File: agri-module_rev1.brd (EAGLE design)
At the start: 160 x 100 mm, 38 parts, among them M1 DMG1023, U2 PCA9570, U3 APDS-9960

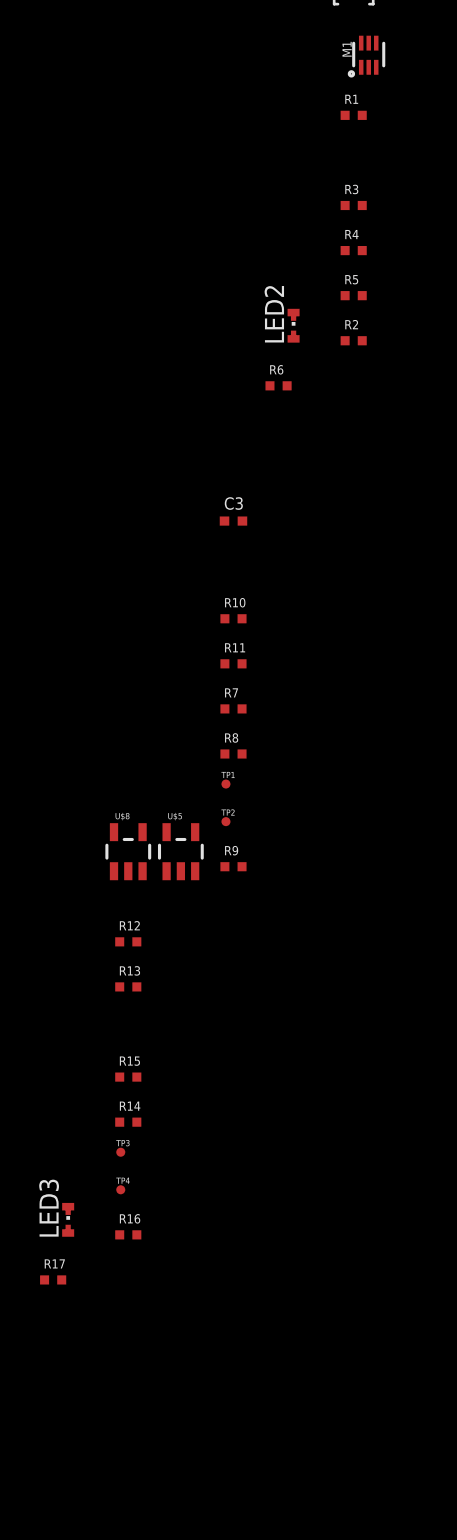
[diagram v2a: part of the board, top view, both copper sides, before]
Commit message: Added indication use for one of LEDs
-also connected EC_pow correctly
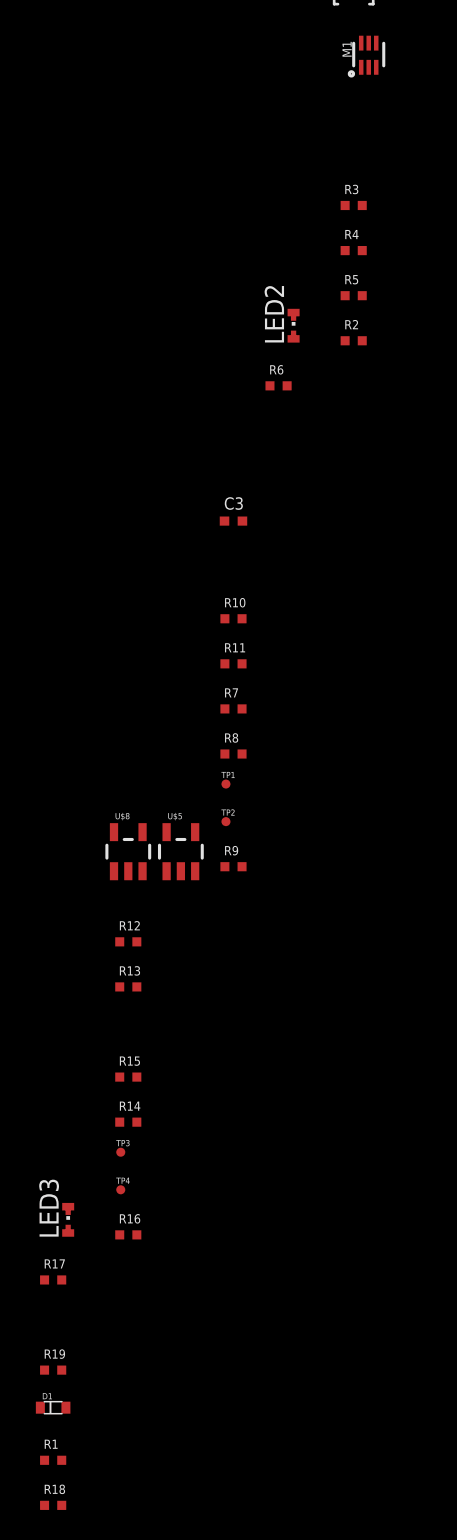
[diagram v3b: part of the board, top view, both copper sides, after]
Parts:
- added D1: DB2S205, EAP - Library:SSMINI2-F5-B
- added R18: 10k, BrainGrid - Resistors:R0402-BG
- added R19: 100R, BrainGrid - Resistors:R0402-BG
- R1: value 100R -> 10k
- moved R1 91.7 mm to (-126.0, -139.0)
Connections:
- removed net N$6: LED2.A@1, U$4.6
- new net LED_INDICATE: D1.C, LED2.A@1, U$4.6
- net 3.6V_HP: now also R1.1, R18.1
- net GEST_LED: now also R19.2, U3.5; no longer R1.2
- net N$4: now also D1.A, R19.1; no longer R1.1, U3.5
- net N$7: now also R18.2
- net N$8: now also R1.2
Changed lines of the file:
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@@
 <attribute name="VMAX" value="-20V" x="-105" y="-45.5" size="1.778" layer="27" display="off"/>
-</element>
-<element name="R1" library="BrainGrid - Resistors" package="R0402-BG" value="100R" x="-106" y="-49.5">
-<attribute name="MPN" value="RC0402JR-07100RL" x="-106" y="-49.5" size="1.778" layer="27" display="off"/>
-<attribute name="ALTMPN" value="RC1005J101CS" x="-106" y="-49.5" size="1.778" layer="27" display="off"/>
-<attribute name="MANF" value="Yageo" x="-106" y="-49.5" size="1.778" layer="27" display="off"/>
-<attribute name="TEMPCO" value="±100ppm/°C" x="-106" y="-49.5" size="1.778" layer="27" display="off"/>
-<attribute name="VPN" value="311-100JRCT-ND" x="-106" y="-49.5" size="1.778" layer="27" display="off"/>
-<attribute name="VENDOR" value="Digikey" x="-106" y="-49.5" size="1.778" layer="27" display="off"/>
-<attribute name="ALTMANF" value="Samsung" x="-106" y="-49.5" size="1.778" layer="27" display="off"/>
-<attribute name="PACKAGE" value="0402" x="-106" y="-49.5" size="1.778" layer="27" display="off"/>
-<attribute name="POPULATE" value="" x="-106" y="-49.5" size="1.778" layer="27" display="off"/>
-<attribute name="TOLERANCE" value="±5%" x="-106" y="-49.5" size="1.778" layer="27" display="off"/>
 </element>
 <element name="R3" library="BrainGrid - Resistors" package="R0402-BG" value="10k" x="-106" y="-55.5">
@@
 <attribute name="POPULATE" value="DNP" x="-126" y="-127" size="1.778" layer="27" display="off"/>
 <attribute name="TOLERANCE" value="" x="-126" y="-127" size="1.778" layer="27" display="off"/>
+</element>
+<element name="R19" library="BrainGrid - Resistors" package="R0402-BG" value="100R" x="-126" y="-133">
+<attribute name="MPN" value="RC0402JR-07100RL" x="-126" y="-133" size="1.778" layer="27" display="off"/>
+<attribute name="ALTMPN" value="RC1005J101CS" x="-126" y="-133" size="1.778" layer="27" display="off"/>
+<attribute name="MANF" value="Yageo" x="-126" y="-133" size="1.778" layer="27" display="off"/>
+<attribute name="TEMPCO" value="±100ppm/°C" x="-126" y="-133" size="1.778" layer="27" display="off"/>
+<attribute name="VPN" value="311-100JRCT-ND" x="-126" y="-133" size="1.778" layer="27" display="off"/>
+<attribute name="VENDOR" value="Digikey" x="-126" y="-133" size="1.778" layer="27" display="off"/>
+<attribute name="ALTMANF" value="Samsung" x="-126" y="-133" size="1.778" layer="27" display="off"/>
+<attribute name="PACKAGE" value="0402" x="-126" y="-133" size="1.778" layer="27" display="off"/>
+<attribute name="POPULATE" value="DNP" x="-126" y="-133" size="1.778" layer="27" display="off"/>
+<attribute name="TOLERANCE" value="±5%" x="-126" y="-133" size="1.778" layer="27" display="off"/>
+</element>
+<element name="D1" library="EAP - Library" package="SSMINI2-F5-B" value="DB2S205" x="-126" y="-135.5">
+<attribute name="MPN" value="" x="-126" y="-135.5" size="1.778" layer="27" display="off"/>
+<attribute name="HEIGHT" value="" x="-126" y="-135.5" size="1.778" layer="27" display="off"/>
+<attribute name="ALTMPN" value="" x="-126" y="-135.5" size="1.778" layer="27" display="off"/>
+<attribute name="MANF" value="" x="-126" y="-135.5" size="1.778" layer="27" display="off"/>
+<attribute name="VPN" value="" x="-126" y="-135.5" size="1.778" layer="27" display="off"/>
+<attribute name="VENDOR" value="" x="-126" y="-135.5" size="1.778" layer="27" display="off"/>
+<attribute name="ALTMANF" value="" x="-126" y="-135.5" size="1.778" layer="27" display="off"/>
+<attribute name="PACKAGE" value="" x="-126" y="-135.5" size="1.778" layer="27" display="off"/>
+<attribute name="POPULATE" value="DNP" x="-126" y="-135.5" size="1.778" layer="27" display="off"/>
+<attribute name="DNP" value="" x="-126" y="-135.5" size="1.778" layer="27" display="off"/>
+<attribute name="TOLERANCE" value="" x="-126" y="-135.5" size="1.778" layer="27" display="off"/>
+</element>
+<element name="R1" library="BrainGrid - Resistors" package="R0402-BG" value="10k" x="-126" y="-139">
+<attribute name="MPN" value="RC0402JR-0710KL" x="-126" y="-139" size="1.778" layer="27" display="off"/>
+<attribute name="ALTMPN" value="1622826-4" x="-126" y="-139" size="1.778" layer="27" display="off"/>
+<attribute name="MANF" value="Yageo" x="-126" y="-139" size="1.778" layer="27" display="off"/>
+<attribute name="TEMPCO" value="±100ppm/°C" x="-126" y="-139" size="1.778" layer="27" display="off"/>
+<attribute name="VPN" value="311-10KJRCT-ND" x="-126" y="-139" size="1.778" layer="27" display="off"/>
+<attribute name="VENDOR" value="Digikey" x="-126" y="-139" size="1.778" layer="27" display="off"/>
+<attribute name="ALTMANF" value="TE" x="-126" y="-139" size="1.778" layer="27" display="off"/>
+<attribute name="PACKAGE" value="0402" x="-126" y="-139" size="1.778" layer="27" display="off"/>
+<attribute name="POPULATE" value="" x="-126" y="-139" size="1.778" layer="27" display="off"/>
+<attribute name="TOLERANCE" value="±5%" x="-126" y="-139" size="1.778" layer="27" display="off"/>
+</element>
+<element name="R18" library="BrainGrid - Resistors" package="R0402-BG" value="10k" x="-126" y="-142">
+<attribute name="MPN" value="RC0402JR-0710KL" x="-126" y="-142" size="1.778" layer="27" display="off"/>
+<attribute name="ALTMPN" value="1622826-4" x="-126" y="-142" size="1.778" layer="27" display="off"/>
+<attribute name="MANF" value="Yageo" x="-126" y="-142" size="1.778" layer="27" display="off"/>
+<attribute name="TEMPCO" value="±100ppm/°C" x="-126" y="-142" size="1.778" layer="27" display="off"/>
+<attribute name="VPN" value="311-10KJRCT-ND" x="-126" y="-142" size="1.778" layer="27" display="off"/>
+<attribute name="VENDOR" value="Digikey" x="-126" y="-142" size="1.778" layer="27" display="off"/>
+<attribute name="ALTMANF" value="TE" x="-126" y="-142" size="1.778" layer="27" display="off"/>
+<attribute name="PACKAGE" value="0402" x="-126" y="-142" size="1.778" layer="27" display="off"/>
+<attribute name="POPULATE" value="" x="-126" y="-142" size="1.778" layer="27" display="off"/>
+<attribute name="TOLERANCE" value="±5%" x="-126" y="-142" size="1.778" layer="27" display="off"/>
 </element>
 </elements>
@@
 <contactref element="U$2" pad="3"/>
 <contactref element="U$5" pad="5"/>
+<contactref element="R1" pad="1"/>
+<contactref element="R18" pad="1"/>
 <wire x1="-105.43" y1="-64.5" x2="-118.45" y2="-97.1999" width="0" layer="19" extent="1-1"/>
 <wire x1="-105.43" y1="-61.5" x2="-105.43" y2="-64.5" width="0" layer="19" extent="1-1"/>
@@
 <wire x1="-98.405" y1="-19.5" x2="-102.6" y2="-39.45" width="0" layer="19" extent="1-1"/>
 <wire x1="-67.405" y1="-1.5" x2="-98.405" y2="-19.5" width="0" layer="19" extent="1-1"/>
+<wire x1="-126.57" y1="-139" x2="-118.45" y2="-97.1999" width="0" layer="19" extent="1-1"/>
+<wire x1="-126.57" y1="-142" x2="-126.57" y2="-139" width="0" layer="19" extent="1-1"/>
 </signal>
 <signal name="N$18">
@@
 </signal>
 <signal name="EC_POW">
+<contactref element="TP2" pad="TP"/>
 <contactref element="U2" pad="6"/>
-<contactref element="TP2" pad="TP"/>
 <wire x1="-101.4" y1="-40" x2="-114.5" y2="-96.5" width="0" layer="19" extent="1-1"/>
 </signal>
@@
 <wire x1="-105.3" y1="-40.485" x2="-105.3" y2="-41.455" width="0" layer="19" extent="1-1"/>
 </signal>
-<signal name="N$4">
-<contactref element="U3" pad="5"/>
-<contactref element="R1" pad="1"/>
-<wire x1="-106.7" y1="-41.455" x2="-106.57" y2="-49.5" width="0" layer="19" extent="1-1"/>
-</signal>
 <signal name="N$5">
 <contactref element="U$4" pad="7"/>
@@
 <wire x1="-32.5" y1="-15.3" x2="-40.5" y2="-19.5" width="0" layer="19" extent="1-1"/>
 </signal>
-<signal name="N$6">
+<signal name="LED_INDICATE">
 <contactref element="U$4" pad="6"/>
 <contactref element="LED2" pad="A@1"/>
+<contactref element="D1" pad="C"/>
+<wire x1="-126.85" y1="-135.5" x2="-110" y2="-64" width="0" layer="19" extent="1-1"/>
 <wire x1="-32" y1="-15.3" x2="-110" y2="-64" width="0" layer="19" extent="1-1"/>
 </signal>
@@
 <contactref element="U$2" pad="6"/>
 <contactref element="U$6" pad="8"/>
+<contactref element="R1" pad="2"/>
 <wire x1="-88.05" y1="-21.825" x2="-94.595" y2="-19.5" width="0" layer="19" extent="1-1"/>
+<wire x1="-125.43" y1="-139" x2="-88.05" y2="-21.825" width="0" layer="19" extent="1-1"/>
 </signal>
 <signal name="N$7">
 <contactref element="U$6" pad="7"/>
 <contactref element="U$2" pad="4"/>
+<contactref element="R18" pad="2"/>
 <wire x1="-87.325" y1="-21.825" x2="-97.135" y2="-19.5" width="0" layer="19" extent="1-1"/>
+<wire x1="-125.43" y1="-142" x2="-97.135" y2="-19.5" width="0" layer="19" extent="1-1"/>
 </signal>
 <signal name="N$10">
@@
 <signal name="GEST_LED">
 <contactref element="U2" pad="4"/>
-<contactref element="R1" pad="2"/>
-<wire x1="-102" y1="-40.6" x2="-105.43" y2="-49.5" width="0" layer="19" extent="1-1"/>
+<contactref element="R19" pad="2"/>
+<contactref element="U3" pad="5"/>
+<wire x1="-102" y1="-40.6" x2="-106.7" y2="-41.455" width="0" layer="19" extent="1-1"/>
+<wire x1="-125.43" y1="-133" x2="-106.7" y2="-41.455" width="0" layer="19" extent="1-1"/>
 </signal>
 <signal name="N$20">
@@
 <wire x1="-32.5" y1="-19.7" x2="-125" y2="-123.5" width="0" layer="19" extent="1-1"/>
 </signal>
+<signal name="N$4">
+<contactref element="R19" pad="1"/>
+<contactref element="D1" pad="A"/>
+<wire x1="-126.57" y1="-133" x2="-125.15" y2="-135.5" width="0" layer="19" extent="1-1"/>
+</signal>
 </signals>

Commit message: x
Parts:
- moved U$4 155.2 mm to (-129.0, -139.5)
- moved U$2 153.7 mm to (48.0, 24.0), flipped to the bottom
- moved U$1 90.4 mm to (20.0, 19.0)
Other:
- board size 160 x 100 mm -> 40 x 40 mm

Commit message: Initial Board Layout
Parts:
- removed TP1, TP2: TEST_PAD, BrainGrid - Electromechanical:TP06R
- U$2: value RJ45_RA_SMD -> 35RASMT2BHNTRX; device BrainGrid - Electromechanical:RJ45_RA_SMD -> BrainGrid - Electromechanical:35RASMTBHNTRX
- moved R18 245.9 mm to (42.0, 37.5), flipped to the bottom, turned to 270 degrees
- moved R1 238.6 mm to (34.5, 37.5), flipped to the bottom, turned to 270 degrees
- moved U$4 235.1 mm to (36.0, 28.0), flipped to the bottom, turned to 270 degrees
- moved R19 219.0 mm to (12.0, 37.0), flipped to the bottom, turned to 90 degrees
- moved D1 218.2 mm to (12.0, 33.5), flipped to the bottom, turned to 90 degrees
- moved TP4 217.5 mm to (42.0, 22.5), flipped to the bottom
- moved TP3 215.2 mm to (42.0, 21.5), flipped to the bottom
- moved R17 214.2 mm to (33.0, 16.5), flipped to the bottom, turned to 90 degrees
- moved R16 213.9 mm to (32.0, 25.5), flipped to the bottom, turned to 90 degrees
- moved R14 212.4 mm to (40.0, 22.0), flipped to the bottom, turned to 270 degrees
- moved R15 205.0 mm to (32.0, 23.0), flipped to the bottom, turned to 90 degrees
- moved R12 203.6 mm to (38.5, 22.0), flipped to the bottom, turned to 270 degrees
- moved R13 199.5 mm to (32.0, 20.5), flipped to the bottom, turned to 90 degrees
- moved LED3 198.9 mm to (9.00, 24.0), turned to 90 degrees
- moved U$8 197.4 mm to (35.0, 22.5), flipped to the bottom, turned to 270 degrees
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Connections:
- removed net N$12: LED3.C@1, R17.1, R9.2, TP1.TP
- new net EC_SENSE: LED3.C@1, R17.1, R9.2, U$2.1
- net 3.6V_HP: now also C1.1; no longer U$2.3
- net 5V: no longer U$2.1, U$2.2
- net EC_POW: now also U$2.4; no longer TP2.TP
- net GND: now also U$2.5; no longer U$2.7, U$2.8
- net N$7: no longer U$2.4
- net N$8: no longer U$2.6
- net T_SENSE: no longer U$2.5
- net VCC: no longer C1.1
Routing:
- net N$11: track 0.00 -> 36.9 mm
- net GND: track 0.00 -> 25.5 mm
- net N$24: track 0.00 -> 25.0 mm
- net 3.6V_HP: track 0.00 -> 10.5 mm
- net VCC: track 0.00 -> 7.65 mm
- net N$22: track 0.00 -> 6.35 mm
- net N$14: track 0.00 -> 6.03 mm
- net N$21: track 0.00 -> 5.78 mm
- net N$15: track 0.00 -> 4.28 mm
- net N$8: track 0.00 -> 3.66 mm
- net N$23: track 0.00 -> 3.11 mm
- net N$3: track 0.00 -> 2.46 mm
- net N$4: track 0.00 -> 2.08 mm
- net N$20: track 0.00 -> 1.90 mm
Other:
- board size 40 x 40 mm -> 44 x 40 mm
